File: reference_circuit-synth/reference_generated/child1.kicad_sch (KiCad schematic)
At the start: 1 part, among them P1 USB_C_Plug_USB2.0

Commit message: Fix symbol 'at' expression format - always include angle for KiCad compatibility
- Modified s_expression.py to always include angle (even if 0) in symbol at expressions
- Changed from (at x y) to (at x y angle) format as required by KiCad
- Fixes 'need a number for symbol orientation' error when opening schematics
- Simplified formatter by removing old complex formatting logic with 15+ boolean flags
- Now using only clean, rule-based formatter (~1800 lines removed)
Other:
- removed sheet child2
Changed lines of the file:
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@@
 		)
 		(instances
-			(project "reference_generated"
-				(path "/e54f82e6-12e8-4c3f-acea-b4b89cde6221/371757ae-7c19-4fd8-b5b8-0cdb4581d496"
+			(project "a5811dcc-4bd3-46a6-b247-f8f8ae0667ae"
+				(path "/a5811dcc-4bd3-46a6-b247-f8f8ae0667ae/ab156568-911d-4c92-962e-68ce032c2d20"
 					(reference "P1")
 					(unit 1)
@@
 		)
 	)
-	(hierarchical_label
-		GND
-		(shape input)
-		(at 120.49000000000001 59.69 0)
-		(effects
-			(font
-				(size 1.27 1.27)
-			)
-			(justify left)
-		)
-	)
-	(sheet
-		(at 81.28 57.15)
-		(size 39.21 20.32)
-		(stroke
-			(width 0.12)
-			(type solid)
-		)
-		(fill
-			(color
-				0
-				0
-				0
-				0.0
-			)
-		)
-		(property "Sheetname" "child2"
-			(at 81.28 55.879999999999995 0)
-			(effects
-				(font
-					(size 1.27 1.27)
-				)
-				(justify left bottom)
-			)
-		)
-		(property "Sheetfile" "child2.kicad_sch"
-			(at 81.28 78.74 0)
-			(effects
-				(font
-					(size 1.27 1.27)
-				)
-				(justify left top)
-				(hide yes)
-			)
-		)
-		(pin
-			GND
-			passive
-			(at 119.22000000000001 59.69 0)
-			(effects
-				(font
-					(size 1.27 1.27)
-				)
-				(justify right)
-			)
-		)
-		(instances
-			(project "reference_generated"
-				(path "/"
-					(page "1")
-				)
-			)
-		)
-	)
-	(text_box
-		"child1 subcircuit\n    Parameters: GND"
-		(exclude_from_sim yes)
-		(at 184.0 110.0 0)
-		(size 80.0 30.0)
-		(margins
-			1.0
-			1.0
-			1.0
-			1.0
-		)
-		(stroke
-			(width 0.1)
-			(type solid)
-		)
-		(fill
-			(type color)
-			(color
-				255
-				255
-				224
-				1
-			)
-		)
-		(effects
-			(font
-				(size 1.2 1.2)
-				(thickness 0.254)
-			)
-			(justify left top)
-		)
-	)
 	(sheet_instances
-		(path "/e54f82e6-12e8-4c3f-acea-b4b89cde6221/371757ae-7c19-4fd8-b5b8-0cdb4581d496"
+		(path "/"
 			(page "1")
 		)

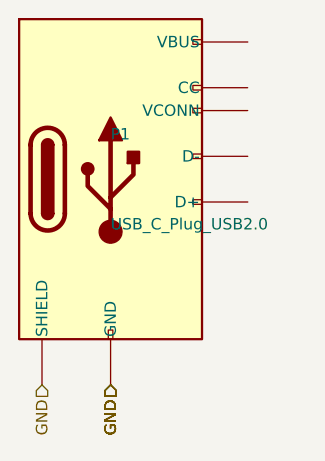
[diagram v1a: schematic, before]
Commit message: Fix lib_symbols population with actual symbol definitions
- Added detailed logging to track lib_symbols generation
- lib_symbols now properly populated with symbol definitions from cache
- Symbol definitions include properties, graphics, and pin information
- Symbols now render correctly in KiCad instead of showing as ?? boxes
- Reference circuit now generates with complete symbol library data
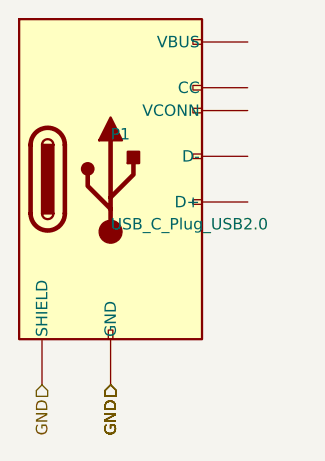
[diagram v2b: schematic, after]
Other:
- company: Circuit-Synth -> (none)
- title: child1 -> (none)
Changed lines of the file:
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@@
 	(version 20250114)
 	(generator "circuit_synth")
-	(generator_version "9.0")
 	(paper "A4")
-	(title_block
-		(title child1)
-		(date 2025-08-08)
-		(company Circuit-Synth)
-	)
 	(symbol
 		(lib_id "Connector:USB_C_Plug_USB2.0")
-		(at 58.42 66.04 0)
+		(at 58.42 66.04 0.0)
 		(unit 1)
 		(exclude_from_sim no)
@@
 		(dnp no)
 		(fields_autoplaced yes)
-		(property "Reference" "P1"
+		(property
+			"Reference"
+			"P1"
 			(at 58.42 61.040000000000006 0)
 			(effects
@@
 			)
 		)
-		(property "Value" "USB_C_Plug_USB2.0"
+		(property
+			"Value"
+			"USB_C_Plug_USB2.0"
 			(at 58.42 71.04 0)
 			(effects
@@
 		)
 		(instances
-			(project "a5811dcc-4bd3-46a6-b247-f8f8ae0667ae"
-				(path "/a5811dcc-4bd3-46a6-b247-f8f8ae0667ae/ab156568-911d-4c92-962e-68ce032c2d20"
+			(project
+				"reference_generated"
+				(path
+					"/a2642601-3cef-41e9-a654-ec36e9238345/3955c852-9b8a-47b6-84be-b5b228043d33"
 					(reference "P1")
 					(unit 1)
@@
 	)
 	(hierarchical_label
-		GND
-		(shape input)
+		"GND"
+		(shape
+			input
+		)
 		(at 50.800000000000004 88.9 270)
 		(effects
@@
 	)
 	(hierarchical_label
-		GND
-		(shape input)
+		"GND"
+		(shape
+			input
+		)
 		(at 58.42 88.9 270)
 		(effects
@@
 	)
 	(hierarchical_label
-		GND
-		(shape input)
+		"GND"
+		(shape
+			input
+		)
 		(at 58.42 88.9 270)
 		(effects
@@
 	)
 	(hierarchical_label
-		GND
-		(shape input)
+		"GND"
+		(shape
+			input
+		)
 		(at 58.42 88.9 270)
 		(effects
@@
 	)
 	(hierarchical_label
-		GND
-		(shape input)
+		"GND"
+		(shape
+			input
+		)
 		(at 58.42 88.9 270)
 		(effects
@@
 	)
 	(sheet_instances
-		(path "/"
-			(page "1")
-		)
 	)
-	(embedded_fonts no)
 )
